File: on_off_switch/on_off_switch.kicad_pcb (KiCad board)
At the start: 2 copper layers, 17 parts, among them K1 HFD23_005-1ZS, Q1 BC846, U1 ATtiny13A-P, U2 L78L05_SOT89

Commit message: added PCB design
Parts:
- U2: footprint Package_SO:SOIC-8_3.9x4.9mm_P1.27mm -> Package_TO_SOT_SMD:SOT-89-3_Handsoldering
- moved C1 24.5 mm to (121.6, 65.6), turned to 90 degrees
- moved C2 18.3 mm to (124.9, 62.3), turned to 180 degrees
- moved U2 14.1 mm to (126.5, 66.4)
- moved U1 13.5 mm to (139.7, 63.1), turned to -90 degrees
- moved D1 12.5 mm to (129.7, 59.7)
- moved PB0 12.4 mm to (129.3, 70.8)
- moved R1 10.2 mm to (139.0, 60.9), turned to 180 degrees
- moved PB1 8.61 mm to (127.0, 70.8)
- moved Q1 6.43 mm to (135.6, 59.8), turned to 90 degrees
- moved PB2 4.90 mm to (124.6, 70.8)
- moved PB4 3.57 mm to (119.9, 70.8)
- moved PB5 1.67 mm to (122.3, 70.8)
- moved GND 1.04 mm to (118.6, 62.4)
- moved +12V 0.95 mm to (118.5, 67.6)
- moved K1 0.36 mm to (125.2, 55.5)
- renumbered H4 to +12V, H1 to +12VS, H3 to GND, H2 to MCU, H5 to PB0, H6 to PB1, H7 to PB2, H8 to PB4, H9 to PB5
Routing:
- net GND: track 0.00 -> 30.3 mm
- net +5V: track 0.00 -> 28.9 mm
- net MCU_PIN_AS&G: track 0.00 -> 21.2 mm
- net Net-(U1-~{RESET}/PB5): track 0.00 -> 20.6 mm
- net Net-(U1-PB4): track 0.00 -> 17.8 mm
- net Net-(D1-A): track 0.00 -> 14.9 mm
- net Net-(U1-PB2): track 0.00 -> 14.0 mm
- net +12V: track 0.00 -> 10.6 mm
- net Net-(U1-PB1): track 0.00 -> 8.62 mm
- net 12VSIGNAL_PIN_AS&G: track 0.00 -> 6.44 mm
- net Net-(Q1-B): track 0.00 -> 5.07 mm
- net base_signal: track 0.00 -> 3.74 mm
- net Net-(U1-PB0): track 0.00 -> 2.76 mm
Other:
- board outline added: 25.9 x 24.1 mm

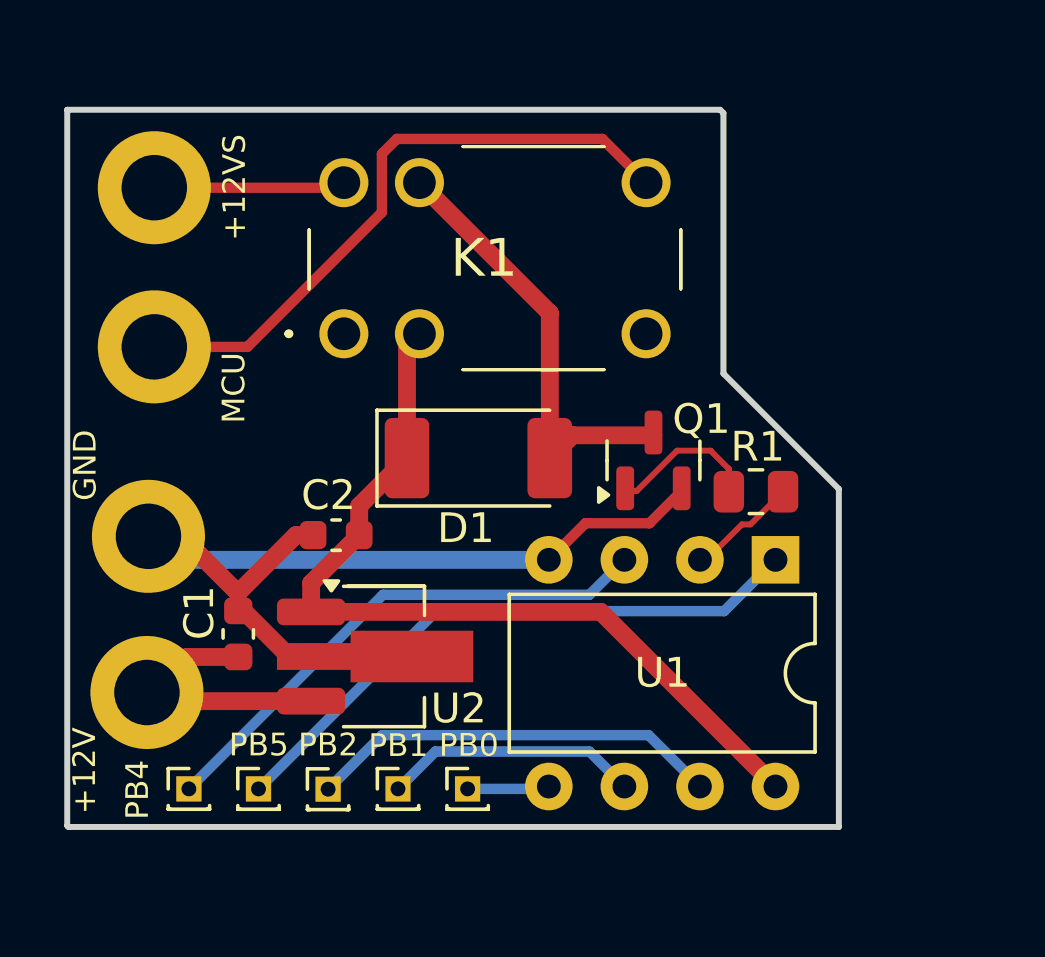
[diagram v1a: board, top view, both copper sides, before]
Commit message: Reworked schematics and PCB
added mounting holes and renamed existing ones.
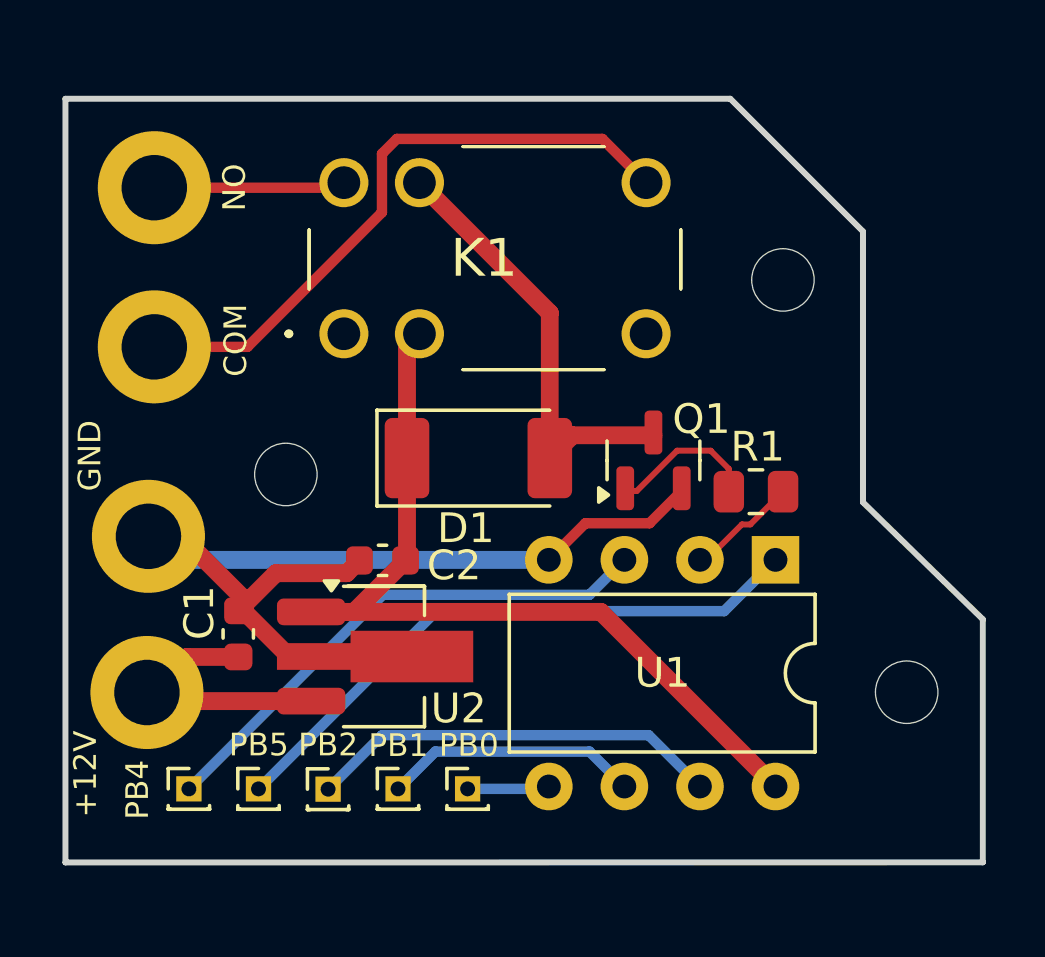
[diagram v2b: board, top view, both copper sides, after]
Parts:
- added H10: MountingHole, MountingHole:MountingHole_2.1mm, F.Cu at (144.1, 67.6)
- added H11: MountingHole, MountingHole:MountingHole_2.1mm, F.Cu at (139.9, 53.7)
- added H12: MountingHole, MountingHole:MountingHole_2.1mm, F.Cu at (123.2, 60.3)
- moved C2 1.78 mm to (126.5, 63.2)
- renumbered MCU to COM, +12VS to NO
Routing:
- net GND: track 30.3 -> 32.2 mm
- net +5V: track 28.9 -> 29.7 mm
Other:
- board size 25.9 x 24.1 mm -> 30.8 x 25.7 mm

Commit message: Schematic and PCB change
Added reverse polarity protection diode, replaced relay diode with 1n4007, removed mounting holes
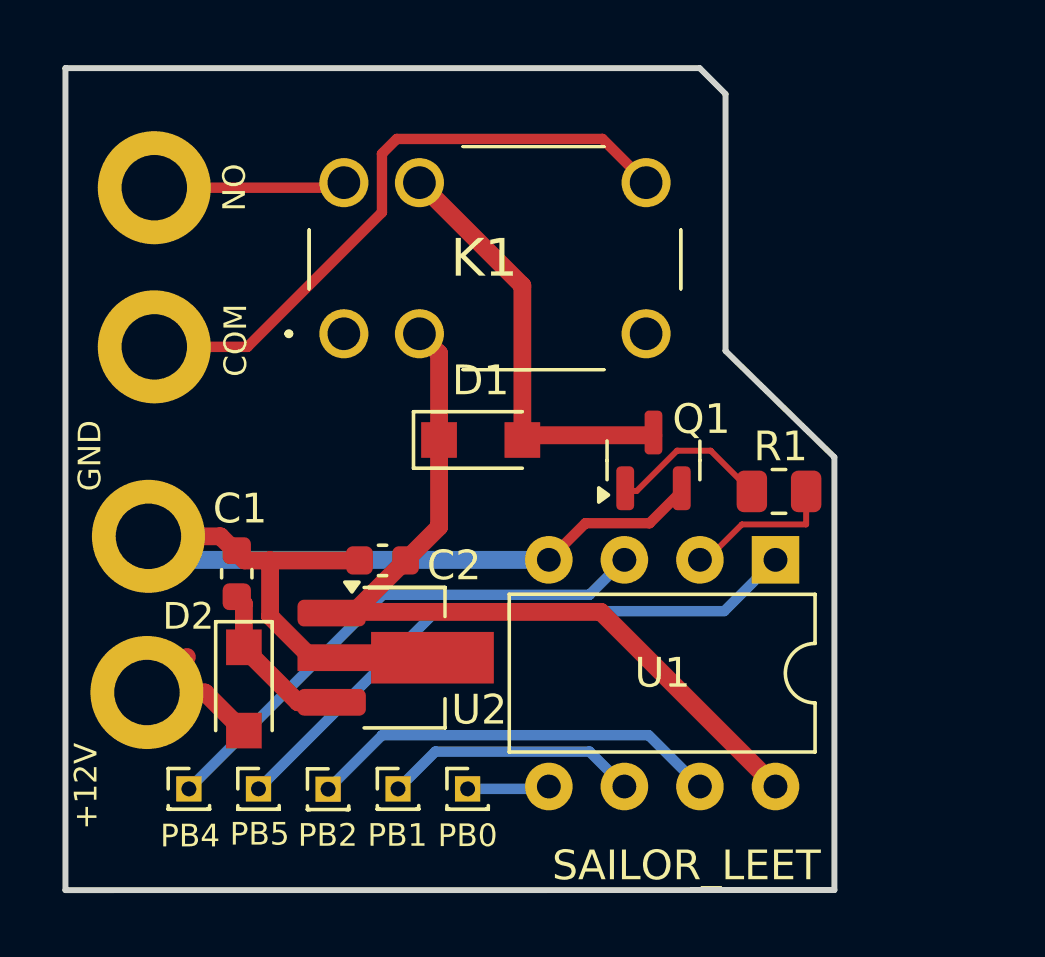
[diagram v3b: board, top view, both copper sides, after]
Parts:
- removed H10, H11, H12: MountingHole, MountingHole:MountingHole_2.1mm
- added D2: 1N4007, Diode_SMD:Nexperia_CFP3_SOD-123W, F.Cu at (121.8, 67.5)
- D1: value SM4007 -> 1N4007; footprint Diode_SMD:D_MELF -> Diode_SMD:Nexperia_CFP3_SOD-123W
- moved C1 2.03 mm to (121.5, 63.6)
- moved R1 0.78 mm to (139.8, 60.8)
- moved U2 0.69 mm to (127.2, 66.4)
- moved D1 0.61 mm to (129.8, 59.1)
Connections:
- C1 pad 1: +12V -> Net-(D2-K)
- U2 pad 3: +12V -> Net-(D2-K)
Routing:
- net Net-(D2-K): track 0.00 -> 5.53 mm
- net +12V: track 10.6 -> 7.41 mm
- net base_signal: track 3.74 -> 5.16 mm
- net +5V: track 29.7 -> 30.3 mm
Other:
- board size 30.8 x 25.7 mm -> 25.8 x 27.6 mm
- board text added: "SAILOR_LEET"

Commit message: Added Gerbers file, modified PCB design
gerber and drill files, minor PCB changes
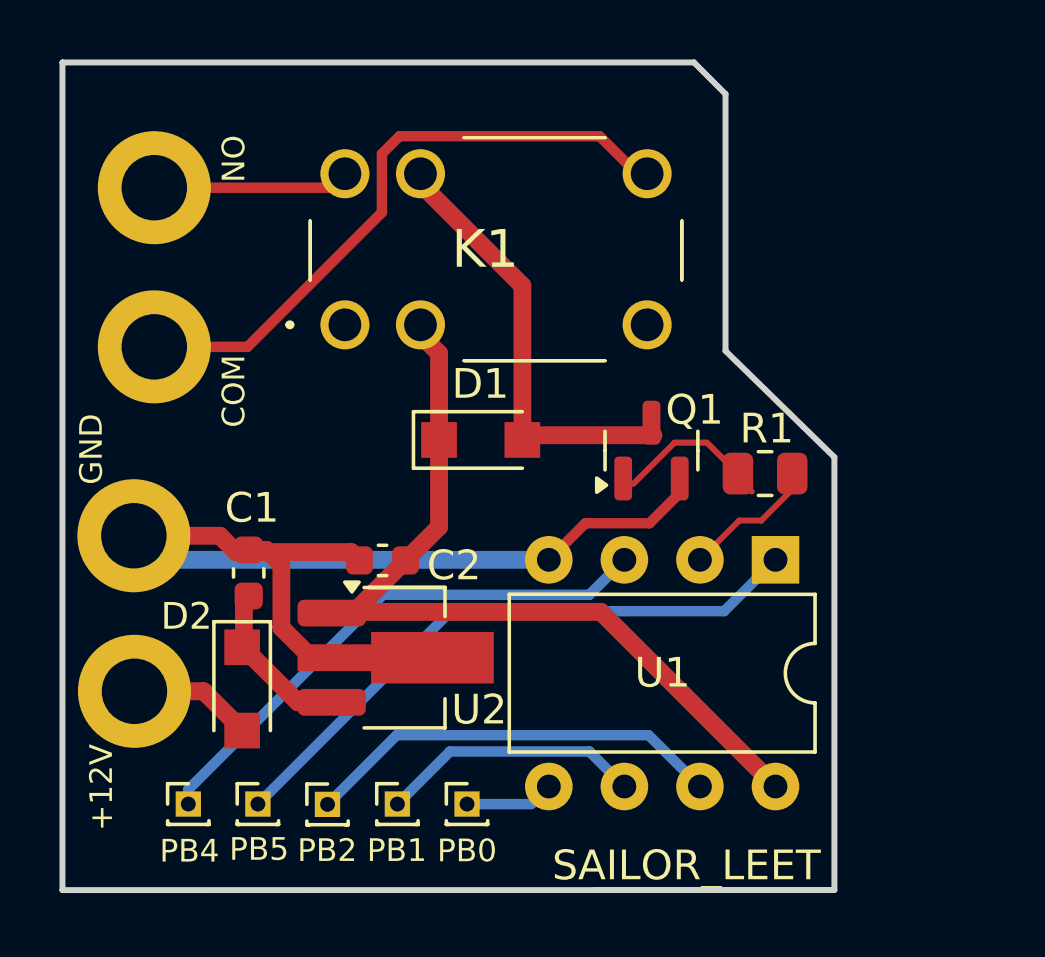
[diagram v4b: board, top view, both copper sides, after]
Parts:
- moved R1 0.76 mm to (139.3, 60.2)
- moved PB2 0.51 mm to (124.6, 71.4)
- moved PB0 0.51 mm to (129.3, 71.3)
- moved PB1 0.51 mm to (127.0, 71.3)
- moved PB4 0.51 mm to (119.9, 71.3)
- moved PB5 0.51 mm to (122.3, 71.3)
- moved GND 0.49 mm to (118.1, 62.3)
- moved +12V 0.42 mm to (118.1, 67.6)
- moved C1 0.40 mm to (122.0, 63.6)
- moved Q1 0.34 mm to (135.5, 59.5)
- moved K1 0.30 mm to (125.2, 55.2)
- moved D2 0.06 mm to (121.7, 67.5)
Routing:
- net +12V: track 7.41 -> 5.62 mm
- net GND: track 32.2 -> 33.2 mm
- net Net-(Q1-B): track 5.39 -> 4.54 mm
- net base_signal: track 5.16 -> 4.62 mm
- net Net-(U1-PB4): track 17.8 -> 18.3 mm
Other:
- board size 25.8 x 27.6 mm -> 25.9 x 27.8 mm
